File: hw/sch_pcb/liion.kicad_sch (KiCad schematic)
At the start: 67 parts, among them Q4 BC807-25, Q7 BSS83P, U1 BQ34Z100, U13 BQ25628E, U2 SN74HC164P

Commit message: Update documentation.
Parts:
- renumbered JP1 to JP5, Q4 to Q5, Q4 to Q6, R1 to R48, R1 to R49, R1 to R52, R1 to R53, R1 to R54, R1 to R55
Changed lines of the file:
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@@
       )
       (project "BATDATUNIT01"
-        (path "/cca3030a-cb35-4155-89c2-3a41e5a0afad"
-          (reference "#PWR015") (unit 1)
-        )
         (path "/cca3030a-cb35-4155-89c2-3a41e5a0afad/ac32fb25-724e-41e3-8a81-e04630a0599b"
           (reference "#PWR0112") (unit 1)
@@
   (symbol (lib_id "Device:Q_PNP_BEC") (at 44.45 77.47 0) (mirror x) (unit 1)
     (in_bom yes) (on_board yes) (dnp no)
-    (property "Reference" "Q4" (at 49.53 78.74 0)
+    (property "Reference" "Q5" (at 49.53 78.74 0)
       (effects (font (size 1 1)) (justify left))
     )
@@
     (instances
       (project "BATDATUNIT01"
-        (path "/cca3030a-cb35-4155-89c2-3a41e5a0afad"
-          (reference "Q4") (unit 1)
-        )
         (path "/cca3030a-cb35-4155-89c2-3a41e5a0afad/ac32fb25-724e-41e3-8a81-e04630a0599b"
           (reference "Q5") (unit 1)
@@
       )
       (project "BATDATUNIT01"
-        (path "/cca3030a-cb35-4155-89c2-3a41e5a0afad"
-          (reference "#PWR015") (unit 1)
-        )
         (path "/cca3030a-cb35-4155-89c2-3a41e5a0afad/ac32fb25-724e-41e3-8a81-e04630a0599b"
           (reference "#PWR0110") (unit 1)
@@
   (symbol (lib_id "Device:R_Small") (at 67.31 173.99 180) (unit 1)
     (in_bom yes) (on_board yes) (dnp no)
-    (property "Reference" "R1" (at 69.85 173.99 90)
+    (property "Reference" "R55" (at 69.85 173.99 90)
       (effects (font (size 1 1)))
     )
@@
     (instances
       (project "BATDATUNIT01"
-        (path "/cca3030a-cb35-4155-89c2-3a41e5a0afad"
-          (reference "R1") (unit 1)
-        )
         (path "/cca3030a-cb35-4155-89c2-3a41e5a0afad/ac32fb25-724e-41e3-8a81-e04630a0599b"
           (reference "R55") (unit 1)
@@
   (symbol (lib_id "Device:R_Small") (at 35.56 77.47 90) (unit 1)
     (in_bom yes) (on_board yes) (dnp no)
-    (property "Reference" "R1" (at 35.56 80.01 90)
+    (property "Reference" "R49" (at 35.56 80.01 90)
       (effects (font (size 1 1)))
     )
@@
     (instances
       (project "BATDATUNIT01"
-        (path "/cca3030a-cb35-4155-89c2-3a41e5a0afad"
-          (reference "R1") (unit 1)
-        )
         (path "/cca3030a-cb35-4155-89c2-3a41e5a0afad/ac32fb25-724e-41e3-8a81-e04630a0599b"
           (reference "R49") (unit 1)
@@
   (symbol (lib_id "power:GND") (at 46.99 54.61 0) (unit 1)
     (in_bom yes) (on_board yes) (dnp no)
-    (property "Reference" "#PWR028" (at 46.99 60.96 0)
+    (property "Reference" "#PWR0109" (at 46.99 60.96 0)
       (effects (font (size 1 1)) hide)
     )
@@
     (instances
       (project "BATDATUNIT01"
-        (path "/cca3030a-cb35-4155-89c2-3a41e5a0afad"
-          (reference "#PWR028") (unit 1)
-        )
         (path "/cca3030a-cb35-4155-89c2-3a41e5a0afad/ac32fb25-724e-41e3-8a81-e04630a0599b"
           (reference "#PWR0109") (unit 1)
@@
   (symbol (lib_id "power:VBUS") (at 115.57 33.02 0) (unit 1)
     (in_bom yes) (on_board yes) (dnp no)
-    (property "Reference" "#PWR013" (at 115.57 36.83 0)
+    (property "Reference" "#PWR0116" (at 115.57 36.83 0)
       (effects (font (size 1 1)) hide)
     )
@@
     (instances
       (project "BATDATUNIT01"
-        (path "/cca3030a-cb35-4155-89c2-3a41e5a0afad"
-          (reference "#PWR013") (unit 1)
-        )
         (path "/cca3030a-cb35-4155-89c2-3a41e5a0afad/ac32fb25-724e-41e3-8a81-e04630a0599b"
           (reference "#PWR0116") (unit 1)
@@
   (symbol (lib_id "power:GND") (at 46.99 96.52 0) (unit 1)
     (in_bom yes) (on_board yes) (dnp no)
-    (property "Reference" "#PWR028" (at 46.99 102.87 0)
+    (property "Reference" "#PWR0111" (at 46.99 102.87 0)
       (effects (font (size 1 1)) hide)
     )
@@
     (instances
       (project "BATDATUNIT01"
-        (path "/cca3030a-cb35-4155-89c2-3a41e5a0afad"
-          (reference "#PWR028") (unit 1)
-        )
         (path "/cca3030a-cb35-4155-89c2-3a41e5a0afad/ac32fb25-724e-41e3-8a81-e04630a0599b"
           (reference "#PWR0111") (unit 1)
@@
       )
       (project "BATDATUNIT01"
-        (path "/cca3030a-cb35-4155-89c2-3a41e5a0afad"
-          (reference "#PWR015") (unit 1)
-        )
         (path "/cca3030a-cb35-4155-89c2-3a41e5a0afad/ac32fb25-724e-41e3-8a81-e04630a0599b"
           (reference "#PWR0108") (unit 1)
@@
   (symbol (lib_id "Device:R_Small") (at 35.56 35.56 90) (unit 1)
     (in_bom yes) (on_board yes) (dnp no)
-    (property "Reference" "R1" (at 35.56 38.1 90)
+    (property "Reference" "R48" (at 35.56 38.1 90)
       (effects (font (size 1 1)))
     )
@@
     (instances
       (project "BATDATUNIT01"
-        (path "/cca3030a-cb35-4155-89c2-3a41e5a0afad"
-          (reference "R1") (unit 1)
-        )
         (path "/cca3030a-cb35-4155-89c2-3a41e5a0afad/ac32fb25-724e-41e3-8a81-e04630a0599b"
           (reference "R48") (unit 1)
@@
   (symbol (lib_id "Jumper:SolderJumper_3_Bridged12") (at 152.4 175.26 270) (unit 1)
     (in_bom yes) (on_board yes) (dnp no)
-    (property "Reference" "JP1" (at 154.94 175.26 0)
+    (property "Reference" "JP5" (at 154.94 175.26 0)
       (effects (font (size 1 1)))
     )
@@
     (instances
       (project "BATDATUNIT01"
-        (path "/cca3030a-cb35-4155-89c2-3a41e5a0afad"
-          (reference "JP1") (unit 1)
-        )
         (path "/cca3030a-cb35-4155-89c2-3a41e5a0afad/ac32fb25-724e-41e3-8a81-e04630a0599b"
           (reference "JP5") (unit 1)
@@
   (symbol (lib_id "Device:R_Small") (at 55.88 157.48 90) (unit 1)
     (in_bom yes) (on_board yes) (dnp no)
-    (property "Reference" "R1" (at 55.88 160.02 90)
+    (property "Reference" "R53" (at 55.88 160.02 90)
       (effects (font (size 1 1)))
     )
@@
     (instances
       (project "BATDATUNIT01"
-        (path "/cca3030a-cb35-4155-89c2-3a41e5a0afad"
-          (reference "R1") (unit 1)
-        )
         (path "/cca3030a-cb35-4155-89c2-3a41e5a0afad/ac32fb25-724e-41e3-8a81-e04630a0599b"
           (reference "R53") (unit 1)
@@
       )
       (project "BATDATUNIT01"
-        (path "/cca3030a-cb35-4155-89c2-3a41e5a0afad"
-          (reference "#PWR015") (unit 1)
-        )
         (path "/cca3030a-cb35-4155-89c2-3a41e5a0afad/ac32fb25-724e-41e3-8a81-e04630a0599b"
           (reference "#PWR0127") (unit 1)
@@
   (symbol (lib_id "Device:R_Small") (at 50.8 152.4 180) (unit 1)
     (in_bom no) (on_board yes) (dnp yes)
-    (property "Reference" "R1" (at 53.34 152.4 90)
+    (property "Reference" "R52" (at 53.34 152.4 90)
       (effects (font (size 1 1)))
     )
@@
     (instances
       (project "BATDATUNIT01"
-        (path "/cca3030a-cb35-4155-89c2-3a41e5a0afad"
-          (reference "R1") (unit 1)
-        )
         (path "/cca3030a-cb35-4155-89c2-3a41e5a0afad/ac32fb25-724e-41e3-8a81-e04630a0599b"
           (reference "R52") (unit 1)
@@
   (symbol (lib_id "power:GND") (at 67.31 177.8 0) (unit 1)
     (in_bom yes) (on_board yes) (dnp no)
-    (property "Reference" "#PWR028" (at 67.31 184.15 0)
+    (property "Reference" "#PWR0114" (at 67.31 184.15 0)
       (effects (font (size 1 1)) hide)
     )
@@
     (instances
       (project "BATDATUNIT01"
-        (path "/cca3030a-cb35-4155-89c2-3a41e5a0afad"
-          (reference "#PWR028") (unit 1)
-        )
         (path "/cca3030a-cb35-4155-89c2-3a41e5a0afad/ac32fb25-724e-41e3-8a81-e04630a0599b"
           (reference "#PWR0114") (unit 1)
@@
           (reference "L1") (unit 1)
         )
-        (path "/cca3030a-cb35-4155-89c2-3a41e5a0afad/c1fc2aff-2b12-4e41-a798-c0c7c2bf1b4c"
-          (reference "L5") (unit 1)
-        )
       )
     )
@@
       )
       (project "BATDATUNIT01"
-        (path "/cca3030a-cb35-4155-89c2-3a41e5a0afad"
-          (reference "#PWR015") (unit 1)
-        )
         (path "/cca3030a-cb35-4155-89c2-3a41e5a0afad/ac32fb25-724e-41e3-8a81-e04630a0599b"
           (reference "#PWR0139") (unit 1)
@@
   (symbol (lib_id "Device:R_Small") (at 67.31 166.37 180) (unit 1)
     (in_bom yes) (on_board yes) (dnp no)
-    (property "Reference" "R1" (at 69.85 166.37 90)
+    (property "Reference" "R54" (at 69.85 166.37 90)
       (effects (font (size 1 1)))
     )
@@
     (instances
       (project "BATDATUNIT01"
-        (path "/cca3030a-cb35-4155-89c2-3a41e5a0afad"
-          (reference "R1") (unit 1)
-        )
         (path "/cca3030a-cb35-4155-89c2-3a41e5a0afad/ac32fb25-724e-41e3-8a81-e04630a0599b"
           (reference "R54") (unit 1)
@@
   (symbol (lib_id "Device:Q_PNP_BEC") (at 44.45 35.56 0) (mirror x) (unit 1)
     (in_bom yes) (on_board yes) (dnp no)
-    (property "Reference" "Q4" (at 49.53 36.83 0)
+    (property "Reference" "Q6" (at 49.53 36.83 0)
       (effects (font (size 1 1)) (justify left))
     )
@@
     (instances
       (project "BATDATUNIT01"
-        (path "/cca3030a-cb35-4155-89c2-3a41e5a0afad"
-          (reference "Q4") (unit 1)
-        )
         (path "/cca3030a-cb35-4155-89c2-3a41e5a0afad/ac32fb25-724e-41e3-8a81-e04630a0599b"
           (reference "Q6") (unit 1)
@@
       )
       (project "BATDATUNIT01"
-        (path "/cca3030a-cb35-4155-89c2-3a41e5a0afad"
-          (reference "#PWR015") (unit 1)
-        )
         (path "/cca3030a-cb35-4155-89c2-3a41e5a0afad/ac32fb25-724e-41e3-8a81-e04630a0599b"
           (reference "#PWR0113") (unit 1)
@@
       )
       (project "BATDATUNIT01"
-        (path "/cca3030a-cb35-4155-89c2-3a41e5a0afad"
-          (reference "#PWR015") (unit 1)
-        )
         (path "/cca3030a-cb35-4155-89c2-3a41e5a0afad/ac32fb25-724e-41e3-8a81-e04630a0599b"
           (reference "#PWR0134") (unit 1)

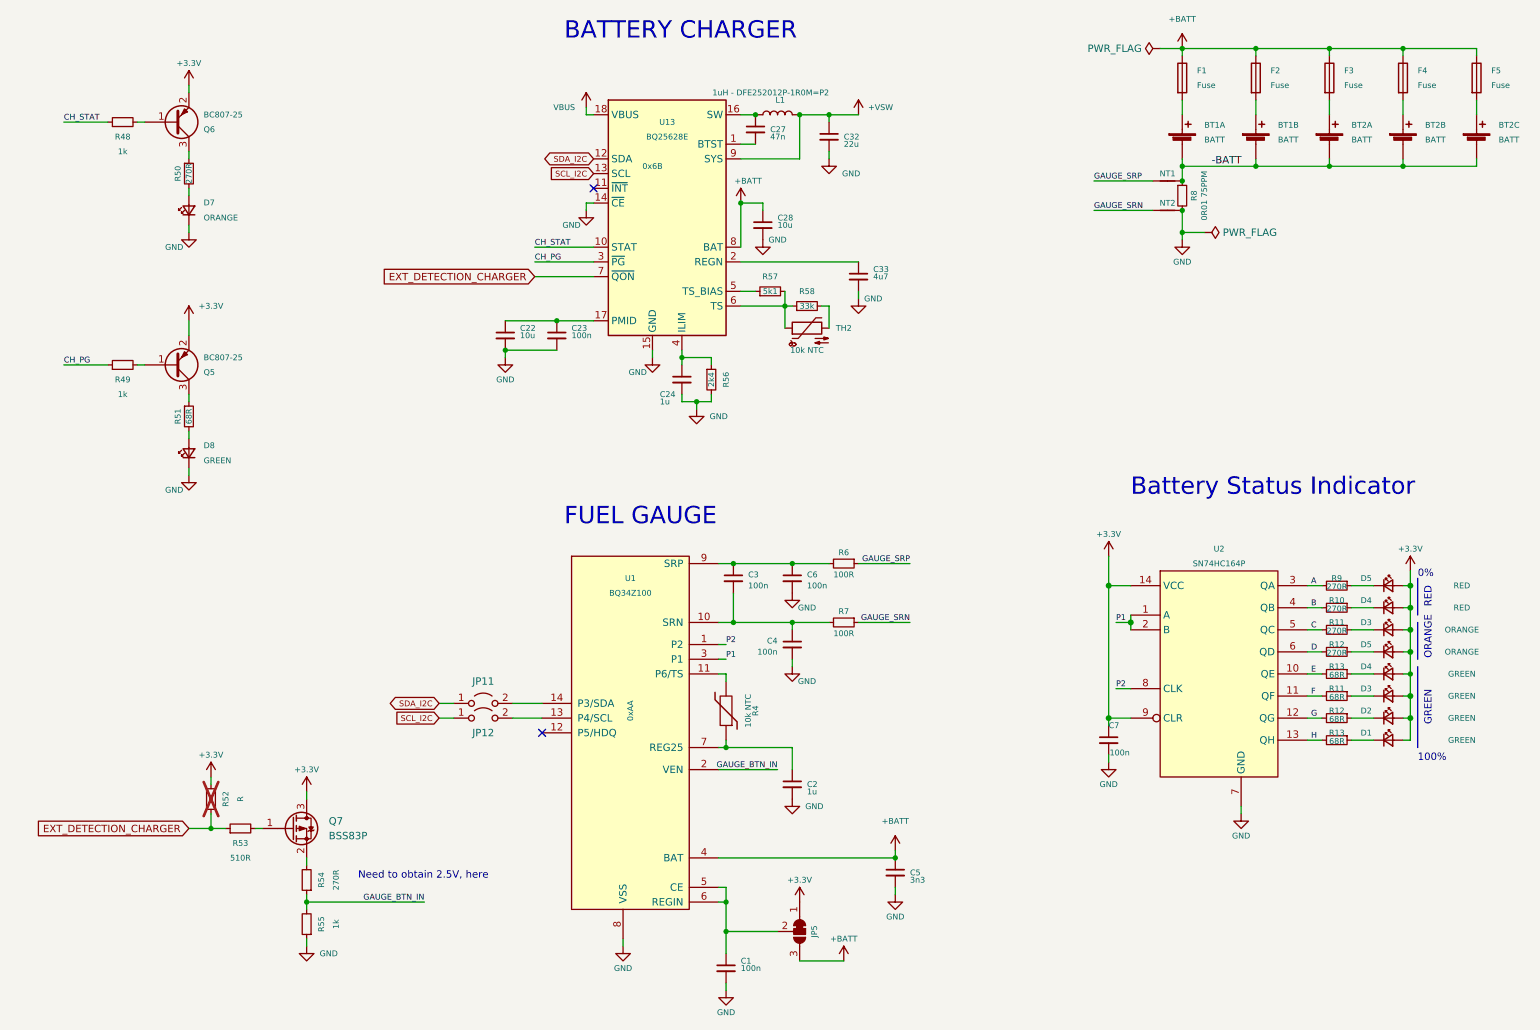
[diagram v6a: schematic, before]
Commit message: Convert to KiCAD 9 Add CR2032 battery holder to avoid RTC reset with removed accumulators.
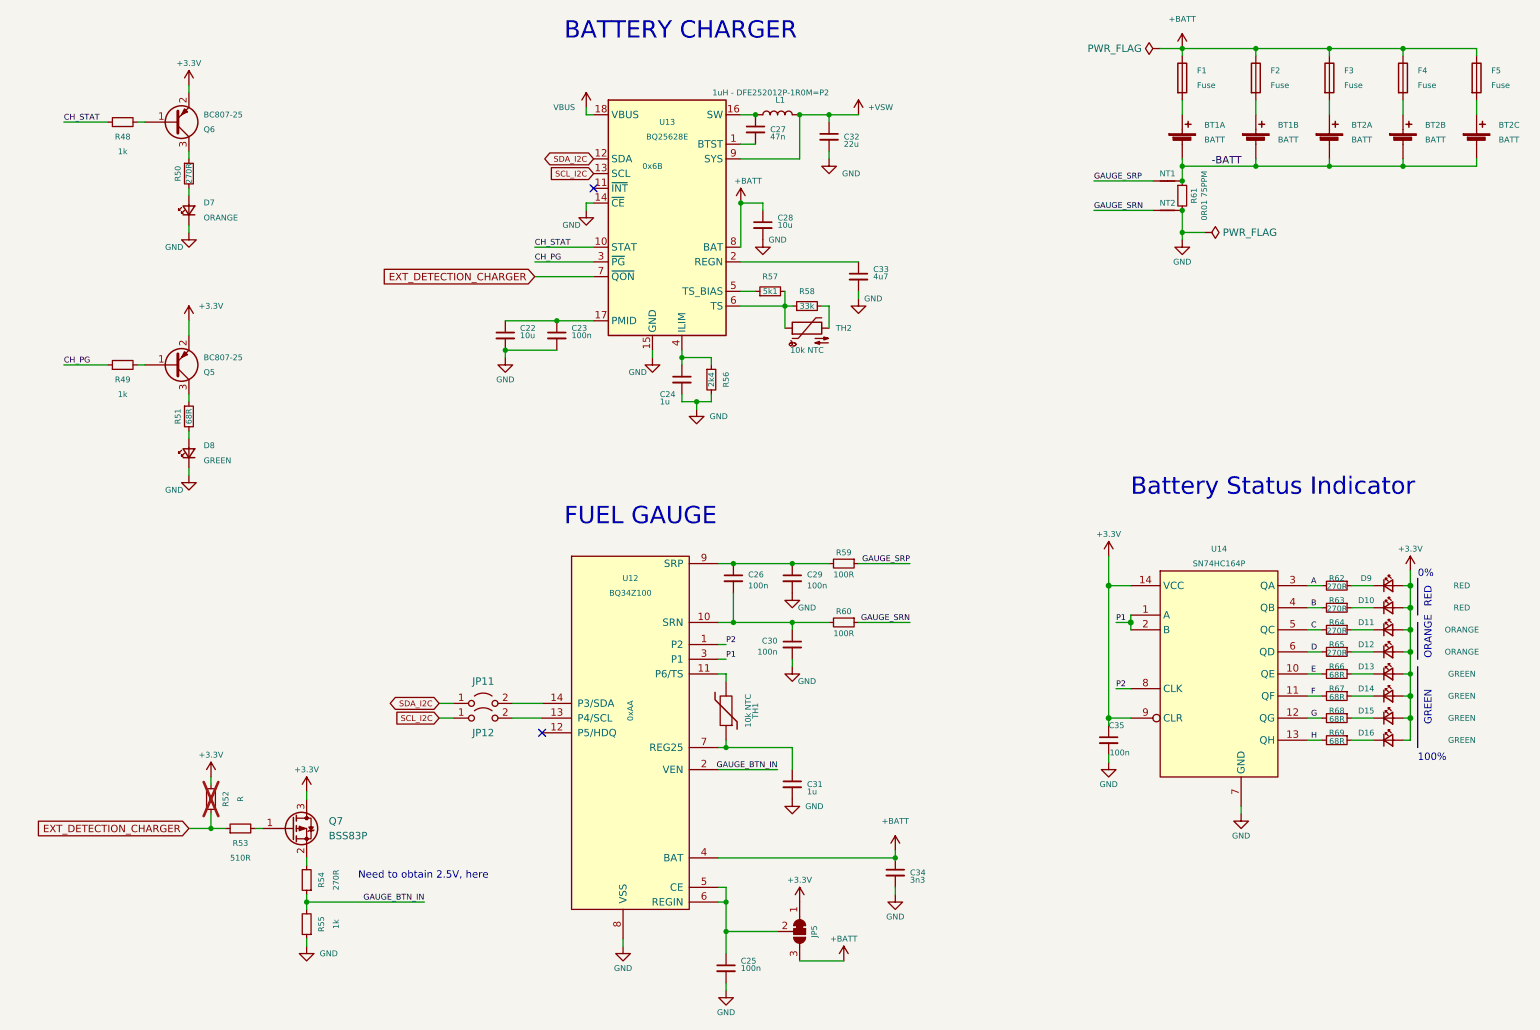
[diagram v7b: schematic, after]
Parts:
- renumbered C1 to C25, C3 to C26, C6 to C29, C4 to C30, C2 to C31, C5 to C34, C7 to C35, D4 to D10, D3 to D11, D5 to D12, D4 to D13, D3 to D14, D2 to D15, D1 to D16, D5 to D9, R6 to R59, R7 to R60, R8 to R61, R9 to R62, R10 to R63, R11 to R64, R12 to R65, R13 to R66, R11 to R67, R12 to R68, R13 to R69, R4 to TH1, U1 to U12, U2 to U14

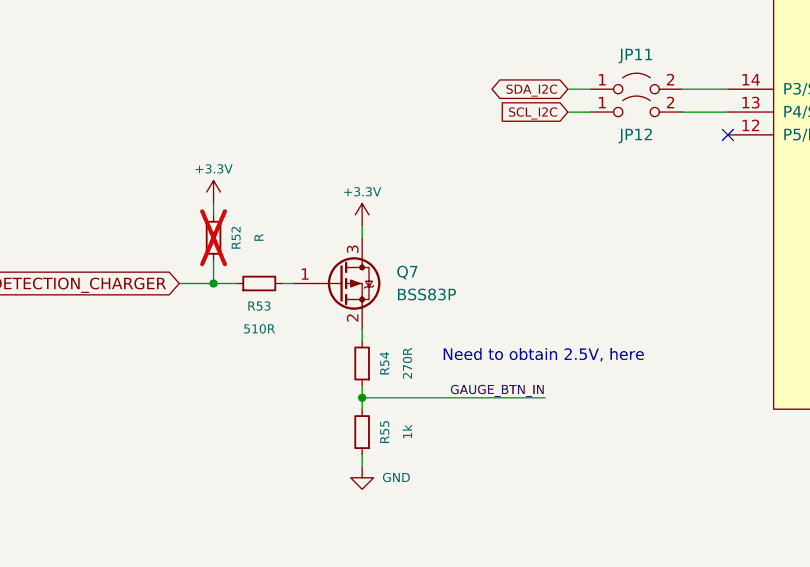
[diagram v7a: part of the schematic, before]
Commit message: Resolve #8 Mirror symbol vertically in schematic.
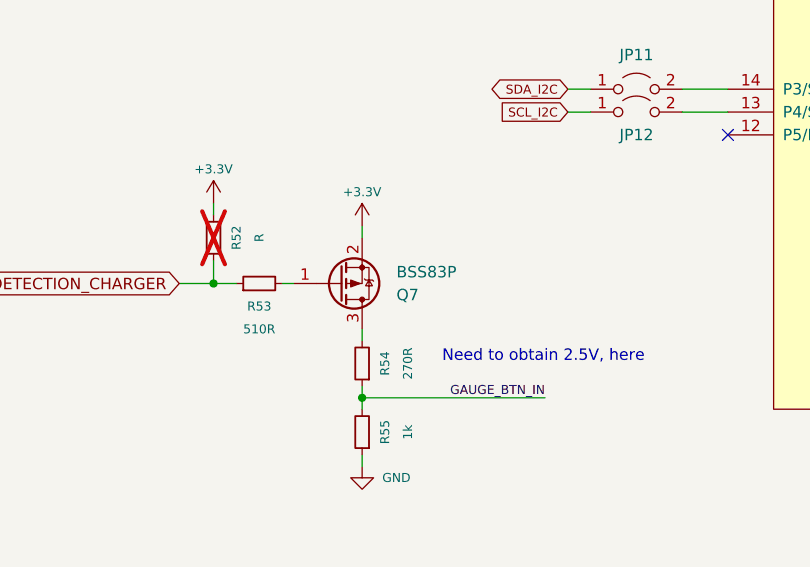
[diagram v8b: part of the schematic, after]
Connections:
- net +3.3V: now also Q7.2 (S); no longer Q7.3 (D)
- net at R54.2: now also Q7.3 (D); no longer Q7.2 (S)
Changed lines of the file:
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@@
 		(lib_id "Device:Q_PMOS_GSD")
 		(at 64.77 157.48 0)
+		(mirror x)
 		(unit 1)
 		(exclude_from_sim no)
@@
 		(on_board yes)
 		(dnp no)
-		(fields_autoplaced yes)
 		(property "Reference" "Q7"
+			(at 71.12 158.75 0)
+			(effects
+				(font
+					(size 1.27 1.27)
+				)
+				(justify left)
+			)
+		)
+		(property "Value" "BSS83P"
 			(at 71.12 156.21 0)
 			(effects
@@
 			)
 		)
-		(property "Value" "BSS83P"
-			(at 71.12 158.75 0)
+		(property "Footprint" "Package_TO_SOT_SMD:SOT-23"
+			(at 69.85 160.02 0)
 			(effects
 				(font
-					(size 1.27 1.27)
-				)
-				(justify left)
-			)
-		)
-		(property "Footprint" "Package_TO_SOT_SMD:SOT-23"
-			(at 69.85 154.94 0)
-			(effects
-				(font
